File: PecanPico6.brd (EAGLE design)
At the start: 44.7 x 12.1 mm, 62 parts, among them IC1 TPS79718DCKT, IC2 SI4463/4, IC4 LPC1114FHN33/333, IC5 SPV1040, IC6 AS213-92LF, IC7 BMP180, Q2 AP2301

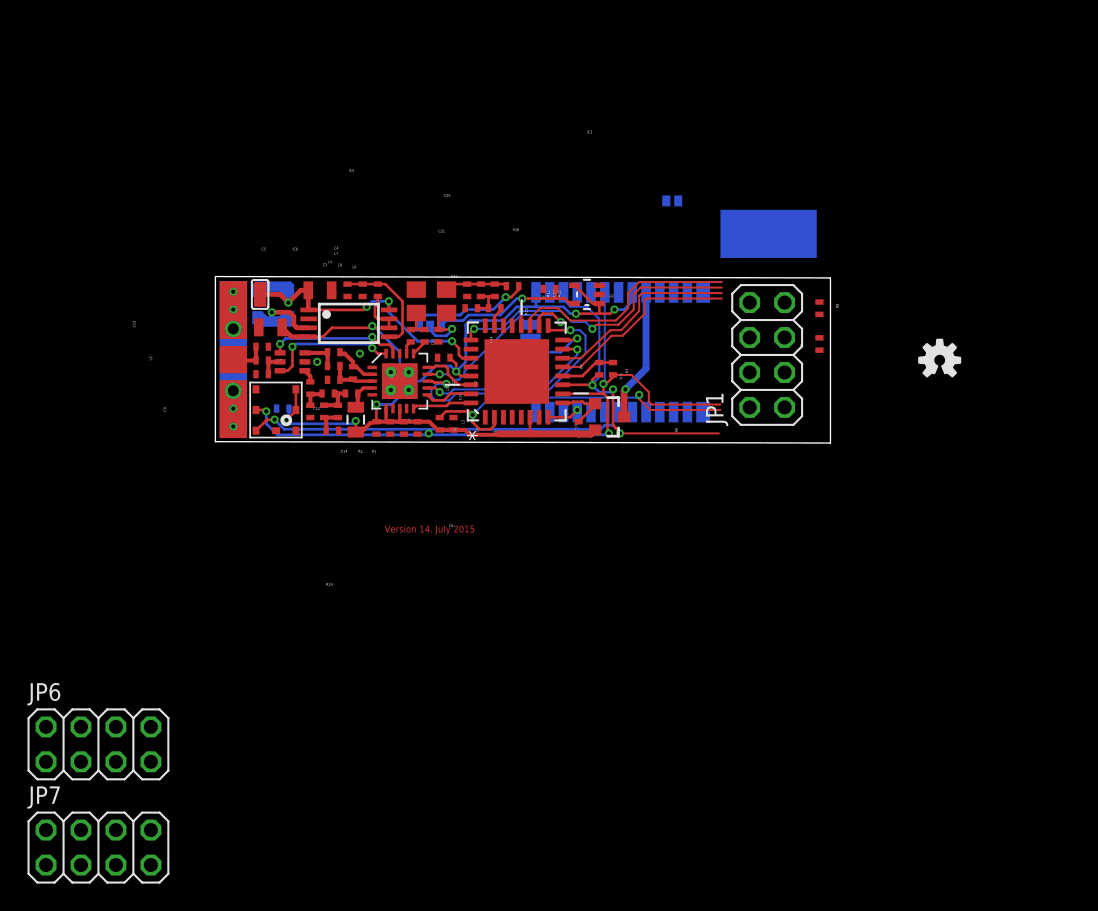
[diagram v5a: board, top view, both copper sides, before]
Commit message: Added programmer jumpers
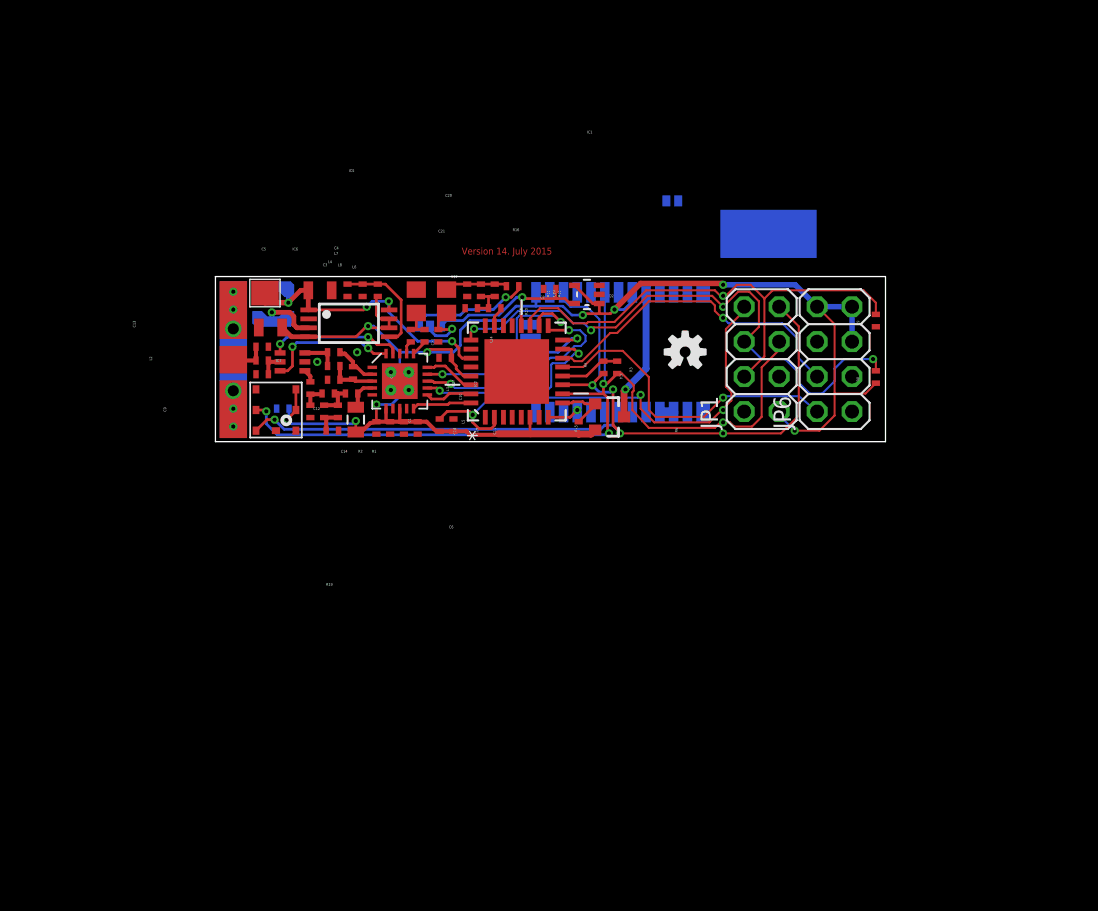
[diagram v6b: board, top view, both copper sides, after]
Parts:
- removed JP3: M01SOLAR, sven:PAD2_1.8X0.9
- removed JP7: (no value), pinhead:2X04
- added JP2: SOLAR, sven:PAD1.8X2.0
- JP4: value M01BATTERY -> BATTERY
- moved JP6 60.4 mm to (46.4, 14.7), turned to 90 degrees
- moved LOGO1 18.5 mm to (35.5, 15.2)
- moved R8 6.47 mm to (49.4, 13.4), turned to 270 degrees
- moved R9 4.44 mm to (49.4, 17.5)
- moved JP1 0.50 mm to (41.1, 14.7)
- moved R3 0.32 mm to (29.6, 14.1)
- moved R4 0.32 mm to (30.6, 14.1)
- moved C20 0.10 mm to (18.1, 14.8)
- moved C6 0.10 mm to (18.7, 9.90)
- moved R15 0.10 mm to (17.7, 9.90)
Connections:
- net GND: now also JP1.2, JP1.3, JP6.1, JP6.3, JP6.6; no longer JP1.6, JP1.7
- net RESET: now also JP1.8; no longer JP1.1
- net RXD: now also JP6.2
- net SCL: now also JP1.5; no longer JP1.4
- net SDA: now also JP1.7; no longer JP1.2
- net SWCLK: now also JP1.4; no longer JP1.5
- net SWDIO: now also JP1.6; no longer JP1.3
- net TXD: now also JP6.4
- net VCC15: now also JP1.1, JP6.5, JP6.7, JP6.8; no longer JP1.8
- net VSOLAR: now also JP2.P$1; no longer JP3.1
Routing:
- net VCC15: track 80.8 -> 119.7 mm, vias 7 -> 9
- net SWDIO: track 21.9 -> 42.0 mm, vias 2 -> 4
- net SWCLK: track 17.0 -> 36.1 mm, vias 0 -> 1
- net SDA: track 51.8 -> 66.8 mm, vias 4 -> 5
- net SCL: track 50.6 -> 61.7 mm, vias 3 -> 4
- net RESET: track 25.0 -> 34.8 mm, vias 2 -> 3
- net TXD: track 14.2 -> 23.7 mm, vias 0 -> 1
- net RXD: track 14.2 -> 23.4 mm, vias 0 -> 1
- net MISO: track 20.5 -> 17.7 mm
- net MOSI: track 14.7 -> 16.0 mm
- net N$2: track 0.00 -> 1.00 mm
- net SCK: track 13.7 -> 14.6 mm
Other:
- board size 44.7 x 12.1 mm -> 48.7 x 12 mm
